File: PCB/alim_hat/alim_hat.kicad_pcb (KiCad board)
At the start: 4 copper layers, 85 x 56 mm, 52 parts, among them J1 Screw_Terminal_01x04, J10 Conn_01x02, J11 Conn_01x02, J12 Conn_01x02, J13 Conn_01x02, J14 Conn_01x02, J15 Conn_01x02, J16 Conn_01x02, J2 XT30, J3 Conn_02x04_Odd_Even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

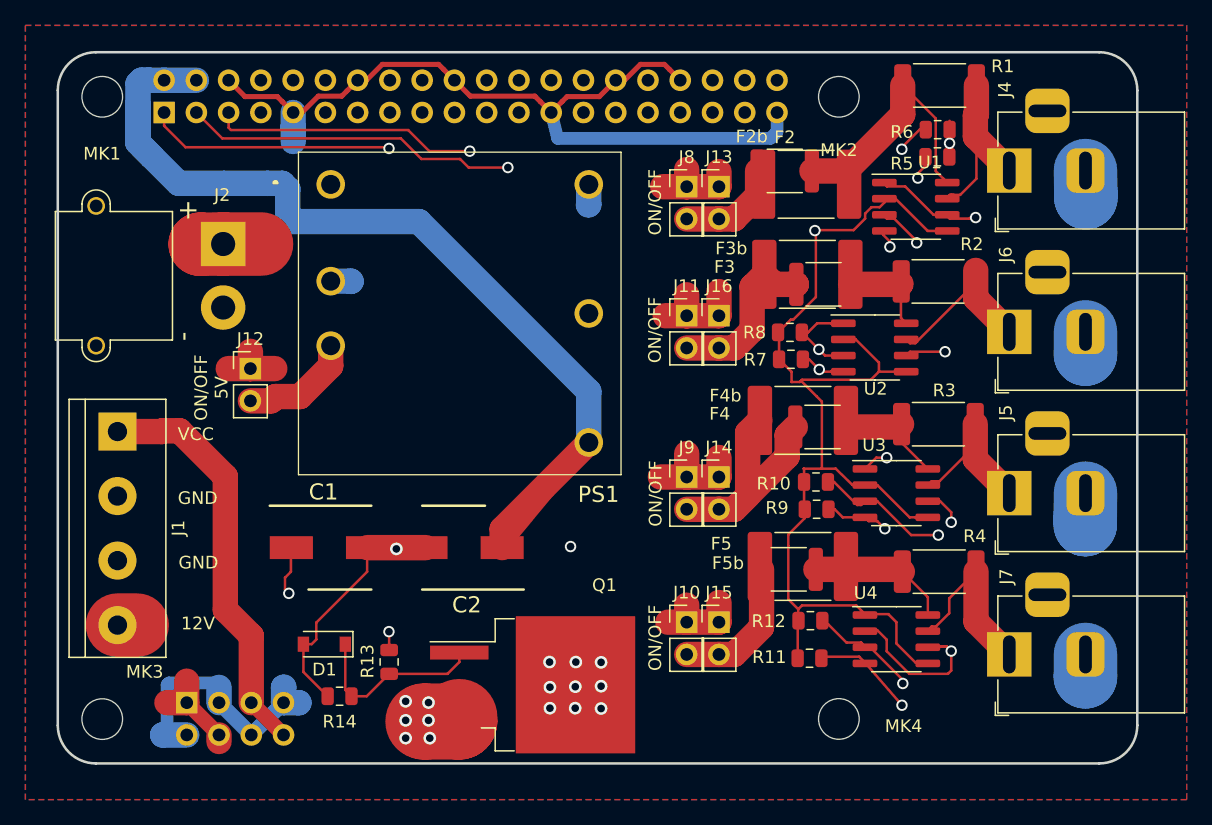
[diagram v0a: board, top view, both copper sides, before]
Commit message: invert polarity xt30 connector
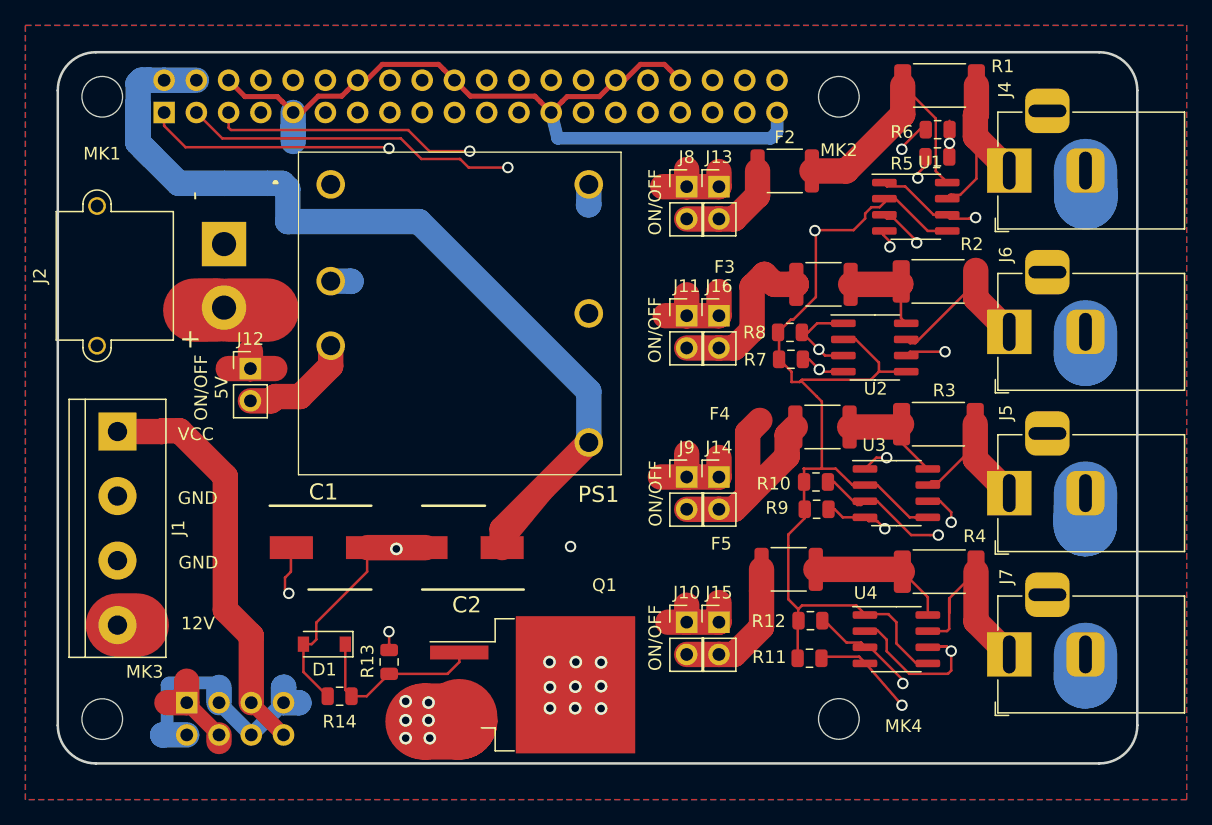
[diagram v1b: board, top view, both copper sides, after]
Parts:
- removed F2b, F3b, F4b, F5b: Fuse_2920_7451Metric, Fuse:Fuse_2920_7451Metric
- C1, C2: value 100uF -> 100uF 35V
- J2: value XT30 -> Conn_01x02_Male
- moved J2 0.07 mm to (213.1, 108.8)
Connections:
- J2 pad 1: +12V -> /gnd_no
- J2 pad 2: /gnd_no -> +12V
- P1 pad 10: (no net) -> /UART_RX
- P1 pad 11: (no net) -> /GPIO17
- P1 pad 12: (no net) -> /GPIO18
- P1 pad 13: (no net) -> /GPIO27
- P1 pad 15: (no net) -> /GPIO22
- P1 pad 16: (no net) -> /GPIO23
- P1 pad 18: (no net) -> /GPIO24
- P1 pad 19: (no net) -> Net-(P1-Pad19)
- P1 pad 21: (no net) -> Net-(P1-Pad21)
- P1 pad 22: (no net) -> /GPIO25
- P1 pad 23: (no net) -> Net-(P1-Pad23)
- P1 pad 24: (no net) -> Net-(P1-Pad24)
- P1 pad 26: (no net) -> Net-(P1-Pad26)
- P1 pad 27: (no net) -> Net-(P1-Pad27)
- P1 pad 28: (no net) -> Net-(P1-Pad28)
- P1 pad 29: (no net) -> /GPIO5
- P1 pad 31: (no net) -> /GPIO6
- P1 pad 32: (no net) -> /GPIO12(PWM0)
- P1 pad 33: (no net) -> /GPIO13(PWM1)
- P1 pad 35: (no net) -> Net-(P1-Pad35)
- P1 pad 36: (no net) -> /GPIO16
- P1 pad 37: (no net) -> /GPIO26
- P1 pad 38: (no net) -> Net-(P1-Pad38)
- P1 pad 40: (no net) -> Net-(P1-Pad40)
- P1 pad 7: (no net) -> /1-wire
- P1 pad 8: (no net) -> /UART_TX
- PS1 pad 1: (no net) -> Net-(PS1-Pad1)
- PS1 pad 5: (no net) -> Net-(PS1-Pad5)
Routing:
- net Net-(J7-Pad1): track 14.8 -> 16.7 mm

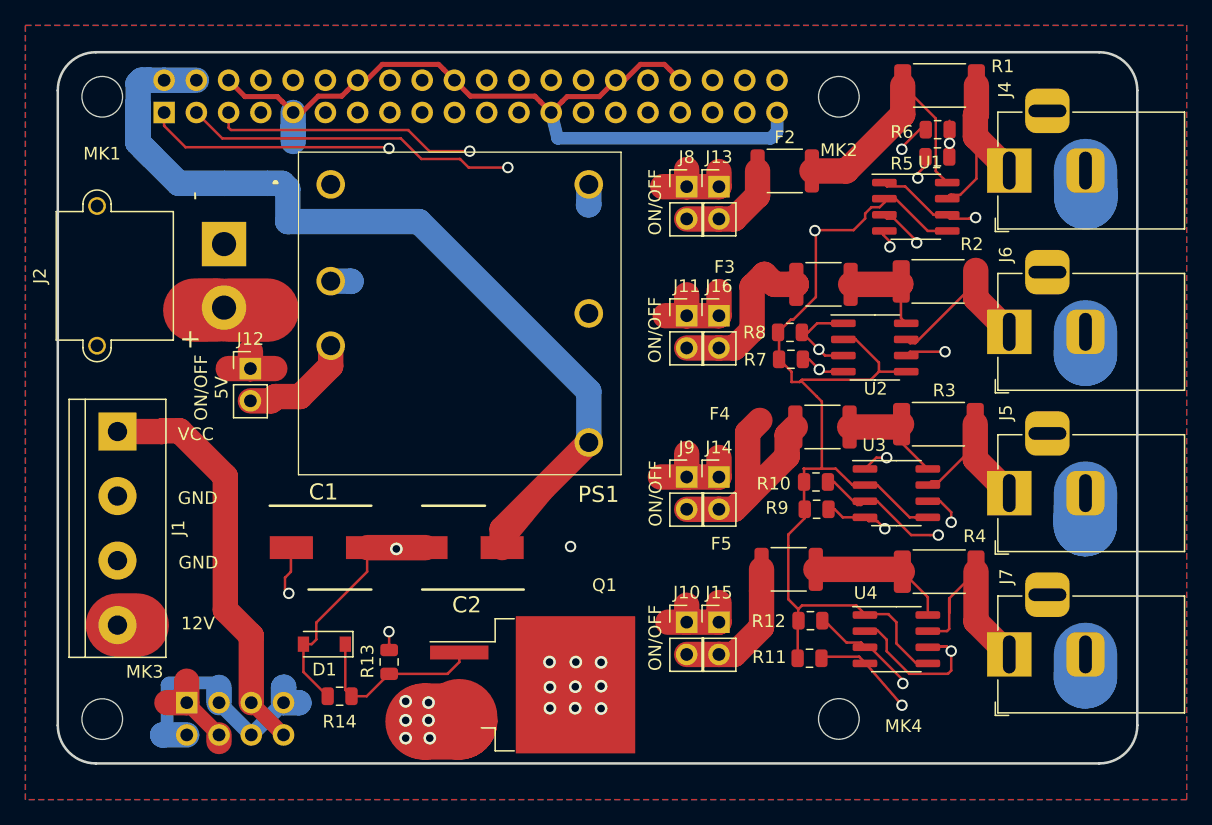
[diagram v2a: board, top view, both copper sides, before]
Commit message: change 12v to GND Jack DC cut-off
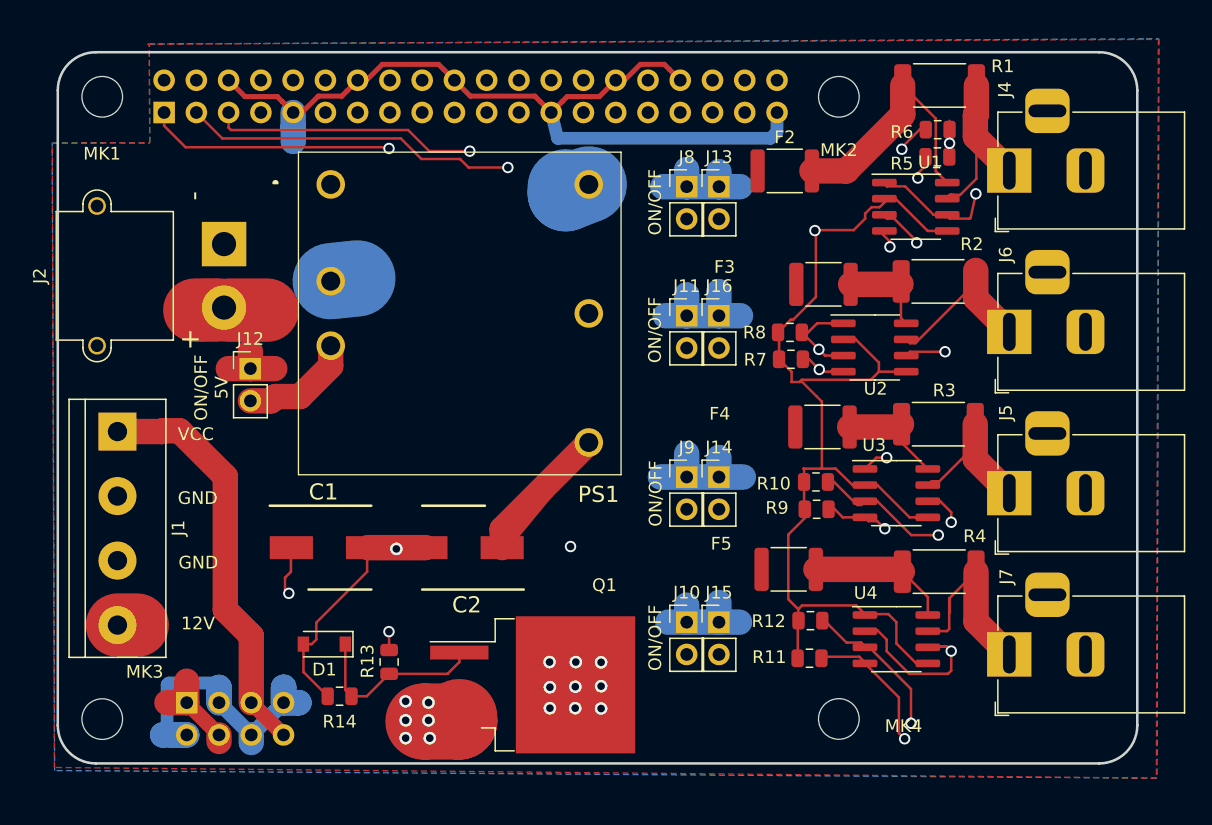
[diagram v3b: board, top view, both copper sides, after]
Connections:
- F2 pad 1: Net-(F2-Pad1) -> +12V
- F3 pad 1: Net-(F3-Pad1) -> +12V
- F4 pad 1: Net-(F4-Pad1) -> +12V
- F5 pad 1: Net-(F5-Pad1) -> +12V
- J10 pad 1: +12V -> GND
- J10 pad 2: Net-(F5-Pad1) -> Net-(J10-Pad2)
- J11 pad 1: +12V -> GND
- J11 pad 2: Net-(F3-Pad1) -> Net-(J11-Pad2)
- J13 pad 1: +12V -> GND
- J13 pad 2: Net-(F2-Pad1) -> Net-(J13-Pad2)
- J14 pad 1: +12V -> GND
- J14 pad 2: Net-(F4-Pad1) -> Net-(J14-Pad2)
- J15 pad 1: +12V -> GND
- J15 pad 2: Net-(F5-Pad1) -> Net-(J10-Pad2)
- J16 pad 1: +12V -> GND
- J16 pad 2: Net-(F3-Pad1) -> Net-(J11-Pad2)
- J4 pad 2: GND -> Net-(J13-Pad2)
- J5 pad 2: GND -> Net-(J14-Pad2)
- J6 pad 2: GND -> Net-(J11-Pad2)
- J7 pad 2: GND -> Net-(J10-Pad2)
- J8 pad 1: +12V -> GND
- J8 pad 2: Net-(F2-Pad1) -> Net-(J13-Pad2)
- J9 pad 1: +12V -> GND
- J9 pad 2: Net-(F4-Pad1) -> Net-(J14-Pad2)
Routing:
- net Net-(J11-Pad2): track 0.00 -> 52.7 mm
- net Net-(J13-Pad2): track 0.00 -> 52.2 mm
- net Net-(J14-Pad2): track 0.00 -> 49.5 mm
- net Net-(J10-Pad2): track 0.00 -> 45.1 mm
- net +12V: track 53.4 -> 25.1 mm
- net Net-(F4-Pad1): track 20.1 -> 0.00 mm
- net GND: track 174.6 -> 193.6 mm
- net Net-(F3-Pad1): track 13.9 -> 0.00 mm
- net Net-(F5-Pad1): track 11.3 -> 0.00 mm
- net Net-(F2-Pad1): track 9.62 -> 0.00 mm
- net /SDA: track 143.0 -> 149.6 mm
- net /SCL: track 131.1 -> 136.7 mm
- net +5V: track 85.1 -> 84.4 mm

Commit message: add pin header for inject 5V in VCC
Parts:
- added J17: Conn_01x02, Connector_PinHeader_2.54mm:PinHeader_1x02_P2.54mm_Vertical, F.Cu at (210.6, 140.8)
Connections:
- P1 pad 10: /UART_RX -> (no net)
- P1 pad 11: /GPIO17 -> (no net)
- P1 pad 12: /GPIO18 -> (no net)
- P1 pad 13: /GPIO27 -> (no net)
- P1 pad 15: /GPIO22 -> (no net)
- P1 pad 16: /GPIO23 -> (no net)
- P1 pad 18: /GPIO24 -> (no net)
- P1 pad 19: Net-(P1-Pad19) -> (no net)
- P1 pad 21: Net-(P1-Pad21) -> (no net)
- P1 pad 22: /GPIO25 -> (no net)
- P1 pad 23: Net-(P1-Pad23) -> (no net)
- P1 pad 24: Net-(P1-Pad24) -> (no net)
- P1 pad 26: Net-(P1-Pad26) -> (no net)
- P1 pad 27: Net-(P1-Pad27) -> (no net)
- P1 pad 28: Net-(P1-Pad28) -> (no net)
- P1 pad 29: /GPIO5 -> (no net)
- P1 pad 31: /GPIO6 -> (no net)
- P1 pad 32: /GPIO12(PWM0) -> (no net)
- P1 pad 33: /GPIO13(PWM1) -> (no net)
- P1 pad 35: Net-(P1-Pad35) -> (no net)
- P1 pad 36: /GPIO16 -> (no net)
- P1 pad 37: /GPIO26 -> (no net)
- P1 pad 38: Net-(P1-Pad38) -> (no net)
- P1 pad 40: Net-(P1-Pad40) -> (no net)
- P1 pad 7: /1-wire -> (no net)
- P1 pad 8: /UART_TX -> (no net)
- PS1 pad 1: Net-(PS1-Pad1) -> (no net)
- PS1 pad 5: Net-(PS1-Pad5) -> (no net)
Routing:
- net +5V: track 84.4 -> 123.0 mm
- net VCC: track 32.3 -> 41.0 mm

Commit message: update gerber for alim hat
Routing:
- net +5V: track 123.0 -> 175.4 mm
- net +12V: track 25.1 -> 30.7 mm
- net GND: track 193.6 -> 199.0 mm
- net Net-(J12-Pad2): track 9.05 -> 8.12 mm
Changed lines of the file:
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@@
     (thickness 1.6)
     (drawings 17)
-    (tracks 538)
+    (tracks 553)
     (zones 0)
     (modules 49)
@@
   )
   (layers
-    (0 F.Cu signal)
-    (1 In1.Cu power)
-    (2 In2.Cu power)
-    (31 B.Cu signal)
+    (0 F.Cu signal hide)
+    (1 In1.Cu power hide)
+    (2 In2.Cu power hide)
+    (31 B.Cu signal hide)
     (32 B.Adhes user hide)
     (33 F.Adhes user hide)
@@
     (add_net +3V3)
     (add_net +5V)
-    (add_net /1-wire)
-    (add_net "/GPIO12(PWM0)")
-    (add_net "/GPIO13(PWM1)")
-    (add_net /GPIO16)
-    (add_net /GPIO17)
-    (add_net /GPIO18)
-    (add_net /GPIO22)
-    (add_net /GPIO23)
-    (add_net /GPIO24)
-    (add_net /GPIO25)
-    (add_net /GPIO26)
-    (add_net /GPIO27)
-    (add_net /GPIO5)
-    (add_net /GPIO6)
     (add_net /SCL)
     (add_net /SDA)
-    (add_net /UART_RX)
-    (add_net /UART_TX)
     (add_net /gnd_no)
     (add_net GND)
@@
     (add_net "Net-(J6-Pad1)")
     (add_net "Net-(J7-Pad1)")
-    (add_net "Net-(P1-Pad19)")
-    (add_net "Net-(P1-Pad21)")
-    (add_net "Net-(P1-Pad23)")
-    (add_net "Net-(P1-Pad24)")
-    (add_net "Net-(P1-Pad26)")
-    (add_net "Net-(P1-Pad27)")
-    (add_net "Net-(P1-Pad28)")
-    (add_net "Net-(P1-Pad35)")
-    (add_net "Net-(P1-Pad38)")
-    (add_net "Net-(P1-Pad40)")
-    (add_net "Net-(PS1-Pad1)")
-    (add_net "Net-(PS1-Pad5)")
     (add_net VCC)
   )
@@
   (segment (start 241.82 120.4) (end 241.82 124.42) (width 2) (layer In1.Cu) (net 2))
   (segment (start 228.45 107.03) (end 241.82 120.4) (width 2) (layer In1.Cu) (net 2))
-  (segment (start 210.55 135.62) (end 210.55 138.3) (width 2) (layer In1.Cu) (net 2))
-  (segment (start 241.82 124.42) (end 221.71 124.42) (width 2) (layer In1.Cu) (net 2))
-  (segment (start 221.71 124.42) (end 210.55 135.62) (width 2) (layer In1.Cu) (net 2))
+  (segment (start 209.719919 95.898) (end 210.922 95.898) (width 2) (layer In2.Cu) (net 2))
+  (segment (start 206.331999 96.74592) (end 207.179919 95.898) (width 2) (layer In2.Cu) (net 2))
+  (segment (start 206.331999 100.248001) (end 206.331999 96.74592) (width 2) (layer In2.Cu) (net 2))
+  (segment (start 206.571999 100.488001) (end 206.331999 100.248001) (width 2) (layer In2.Cu) (net 2))
+  (segment (start 207.179919 95.898) (end 209.719919 95.898) (width 2) (layer In2.Cu) (net 2))
+  (segment (start 212.720605 100.488001) (end 206.571999 100.488001) (width 2) (layer In2.Cu) (net 2))
+  (segment (start 221.627603 109.394999) (end 212.720605 100.488001) (width 2) (layer In2.Cu) (net 2))
+  (segment (start 226.794999 109.394999) (end 221.627603 109.394999) (width 2) (layer In2.Cu) (net 2))
+  (segment (start 241.82 124.42) (end 226.794999 109.394999) (width 2) (layer In2.Cu) (net 2))
+  (segment (start 224.43 124.42) (end 241.82 124.42) (width 2) (layer In2.Cu) (net 2))
+  (segment (start 210.55 138.3) (end 224.43 124.42) (width 2) (layer In2.Cu) (net 2))
   (via (at 229.3 147.7) (size 1) (drill 0.6) (layers F.Cu B.Cu) (net 3))
   (via (at 227.4 147.7) (size 1) (drill 0.6) (layers F.Cu B.Cu) (net 3))
@@
   (segment (start 271.805 106.795) (end 270.245 106.795) (width 0.2) (layer F.Cu) (net 3))
   (segment (start 270.245 106.795) (end 269.945 106.495) (width 0.2) (layer F.Cu) (net 3))
+  (segment (start 217.78508 144.9073) (end 218.987161 144.9073) (width 2) (layer In1.Cu) (net 3))
+  (segment (start 218.999861 144.92) (end 218.987161 144.9073) (width 2) (layer In1.Cu) (net 3))
+  (segment (start 217.78508 144.9073) (end 217.78508 143.705219) (width 2) (layer In1.Cu) (net 3))
+  (segment (start 217.77 143.690139) (end 217.78508 143.705219) (width 2) (layer In1.Cu) (net 3))
+  (segment (start 215.24508 147.99492) (end 215.24508 147.4473) (width 2) (layer In1.Cu) (net 3))
+  (segment (start 212.70508 144.9073) (end 212.70508 143.45508) (width 2) (layer In1.Cu) (net 3))
+  (segment (start 209.2373 147.4473) (end 209.22 147.43) (width 2) (layer In1.Cu) (net 3))
+  (segment (start 210.16508 147.4473) (end 209.22 147.43) (width 2) (layer In1.Cu) (net 3))
   (segment (start 212.7 147.46) (end 212.7 147.705998) (width 1) (layer B.Cu) (net 4))
   (segment (start 215.19682 118.26524) (end 215.19682 118.13824) (width 1) (layer F.Cu) (net 4))
@@
   (segment (start 210.16508 144.9073) (end 212.70508 147.4473) (width 1.2) (layer F.Cu) (net 4))
   (segment (start 255.503 102.887) (end 255.503 101.553) (width 0.2) (layer F.Cu) (net 4))
+  (segment (start 213.1 116.52656) (end 215.1765 118.60306) (width 2) (layer In1.Cu) (net 4))
+  (segment (start 213.1 113.8) (end 213.1 116.52656) (width 2) (layer In1.Cu) (net 4))
   (segment (start 215.24 144.90222) (end 215.24508 144.9073) (width 1) (layer F.Cu) (net 5))
-  (segment (start 215.24508 144.9073) (end 217.78508 147.4473) (width 1.2) (layer F.Cu) (net 5))
   (segment (start 208.27 123.5) (end 209.6 123.5) (width 2) (layer F.Cu) (net 5))
   (segment (start 208.21 123.56) (end 208.27 123.5) (width 2) (layer F.Cu) (net 5))
@@
   (segment (start 210.55 140.84) (end 213.85 140.85) (width 2) (layer In1.Cu) (net 5))
   (segment (start 213.85 140.85) (end 215.24508 142.24508) (width 2) (layer In1.Cu) (net 5))
+  (segment (start 215.24508 144.9073) (end 217.78508 147.4473) (width 1.2) (layer F.Cu) (net 5))
   (segment (start 268.3525 101.91) (end 268.3325 101.93) (width 0.2) (layer F.Cu) (net 6))
   (segment (start 264.454 125.616) (end 265.278 125.616) (width 0.2) (layer F.Cu) (net 6))
@@
   (segment (start 270.2 139.1) (end 270.2 136.7) (width 0.2) (layer F.Cu) (net 15))
   (segment (start 270.025 139.275) (end 270.2 139.1) (width 0.2) (layer F.Cu) (net 15))
-  (segment (start 221.5 118.39099) (end 221.5 116.8) (width 2) (layer F.Cu) (net 16))
-  (segment (start 215.1765 121.14306) (end 216.81001 121.14306) (width 2) (layer F.Cu) (net 16))
-  (segment (start 219.08792 120.80307) (end 221.5 118.39099) (width 2) (layer F.Cu) (net 16))
-  (segment (start 216.81001 121.14306) (end 217.15 120.80307) (width 2) (layer F.Cu) (net 16))
-  (segment (start 217.15 120.80307) (end 219.08792 120.80307) (width 2) (layer F.Cu) (net 16))
+  (segment (start 217.15694 121.14306) (end 221.5 116.8) (width 2) (layer B.Cu) (net 16))
+  (segment (start 215.1765 121.14306) (end 217.15694 121.14306) (width 2) (layer B.Cu) (net 16))
   (via (at 240.75 145.34) (size 1) (drill 0.6) (layers F.Cu B.Cu) (net 17))
   (via (at 240.76 143.65) (size 1) (drill 0.6) (layers F.Cu B.Cu) (net 17))
